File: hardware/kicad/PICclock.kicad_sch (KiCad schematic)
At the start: 25 parts, among them J1 ICSP, J2 CLK_OUT, SW1 VAR/STEP, SW2 HS/[VAR/STEP], SW3 STEP, U1 PIC16F18344-P, U2 74HCT00, U3 EL7232CNZ, Y1 25MHz, Y2 CXO_DIP14

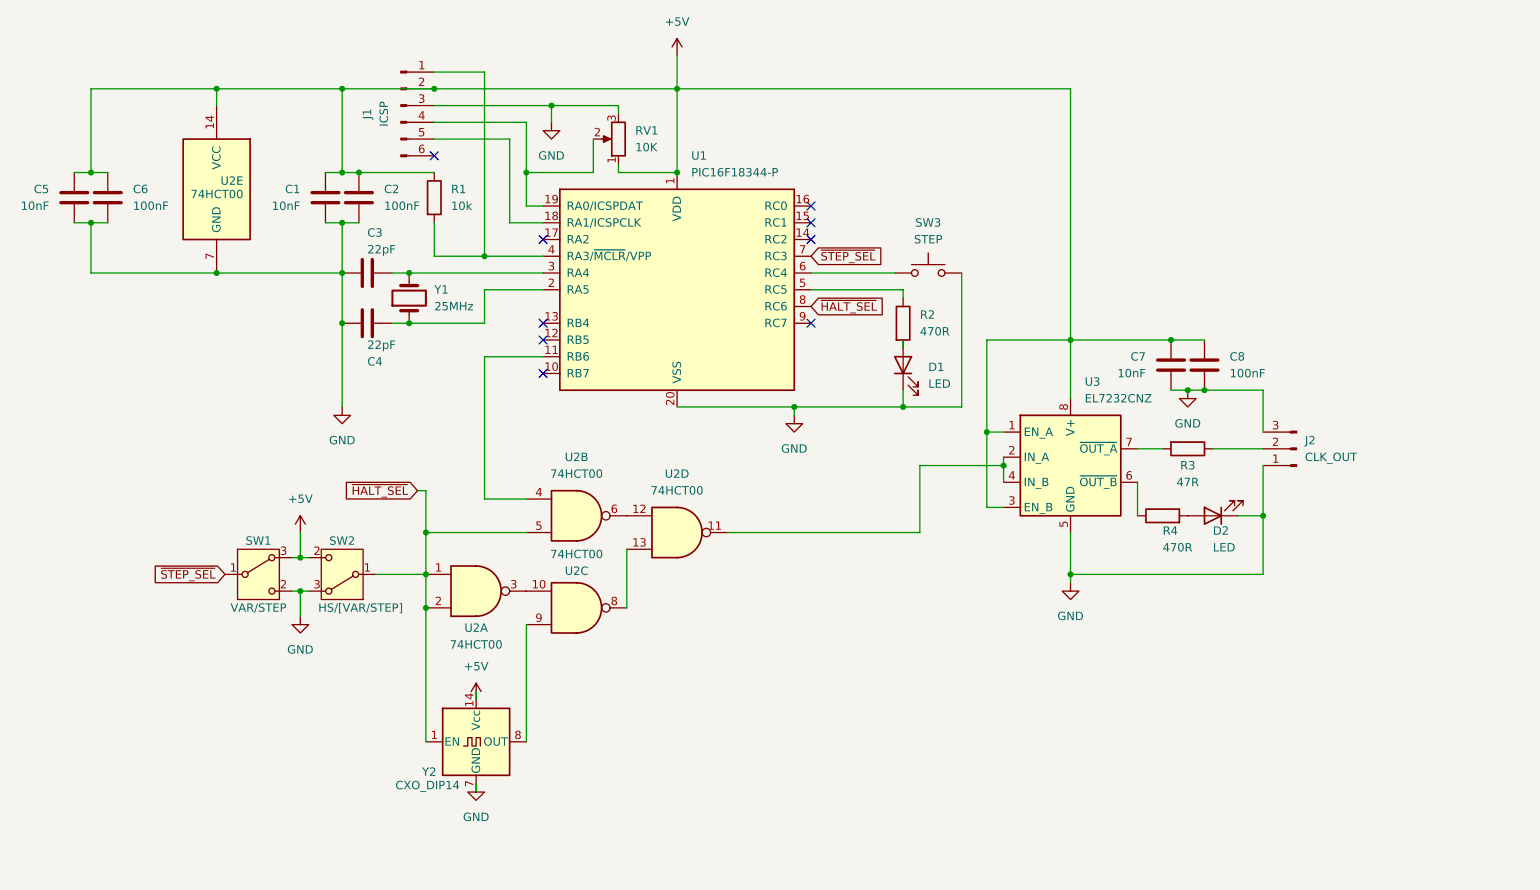
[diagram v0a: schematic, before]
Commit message: add power input
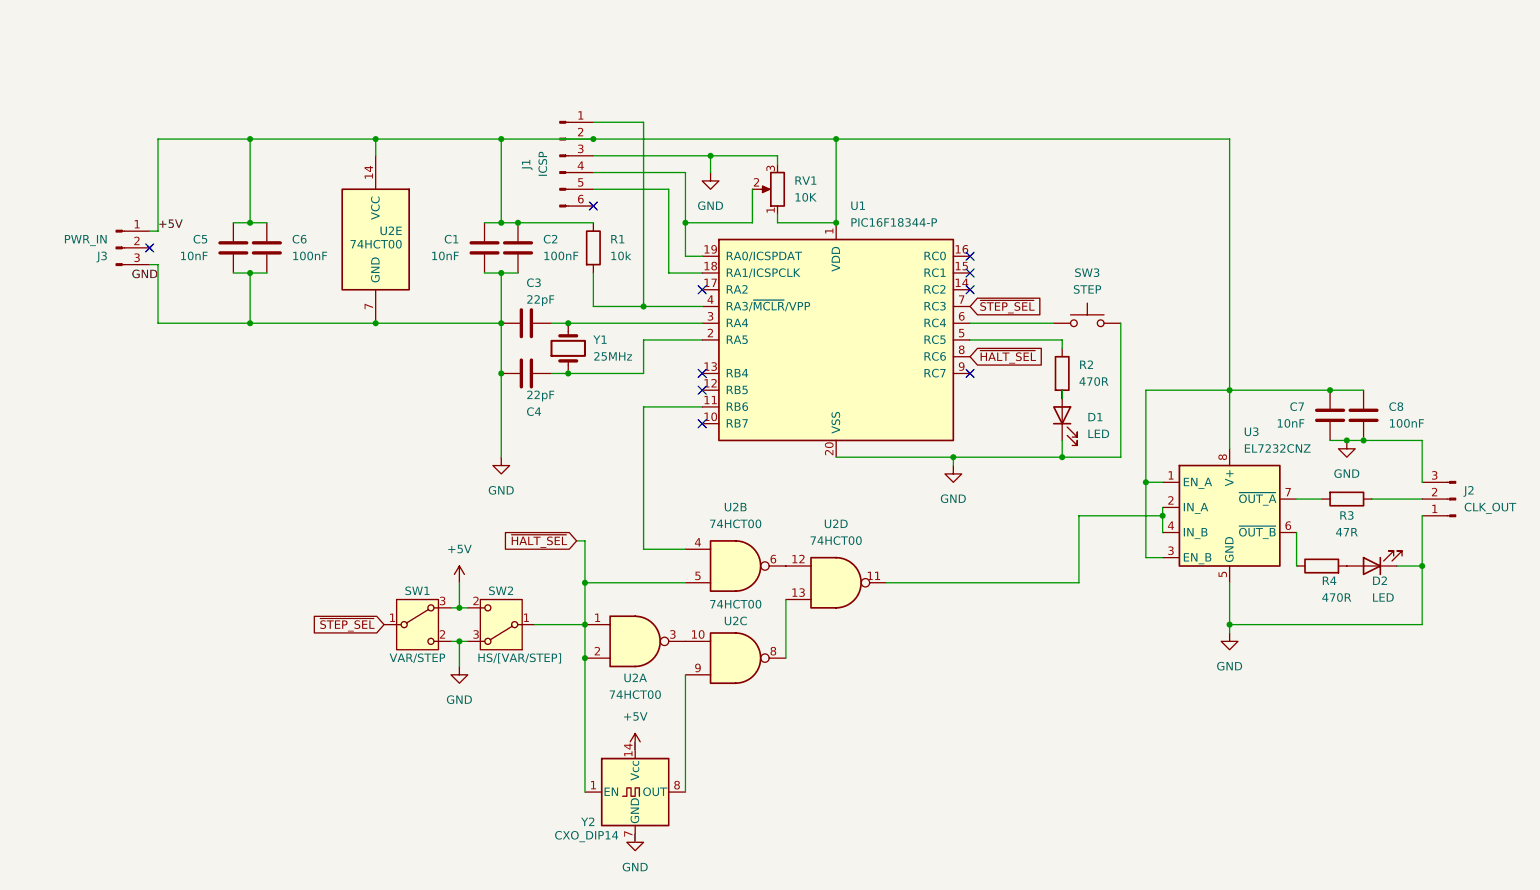
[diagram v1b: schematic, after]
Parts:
- added J3: PWR_IN, Connector_PinHeader_2.54mm:PinHeader_1x03_P2.54mm_Vertical, symbol Connector:Conn_01x03_Pin
- SW3: footprint Connector_PinHeader_2.54mm:PinHeader_1x03_P2.54mm_Vertical -> Button_Switch_Keyboard:SW_Cherry_MX_1.00u_PCB
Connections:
- net +5V: now also J3.1 (Pin_1)
- net GND: now also J3.3 (Pin_3)
- no-connect marks 9 -> 10
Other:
- moved on the sheet: C1, C2, C3, C4, C5, C6, C7, C8, D1, D2, J1, J2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
